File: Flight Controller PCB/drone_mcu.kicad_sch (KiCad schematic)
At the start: 24 parts, among them J2 JTAG, SW1 SW_Push, SW2 SW_SPDT, U2 STM32F411RETx, Y1 32.768kHz, Y2 25MHz

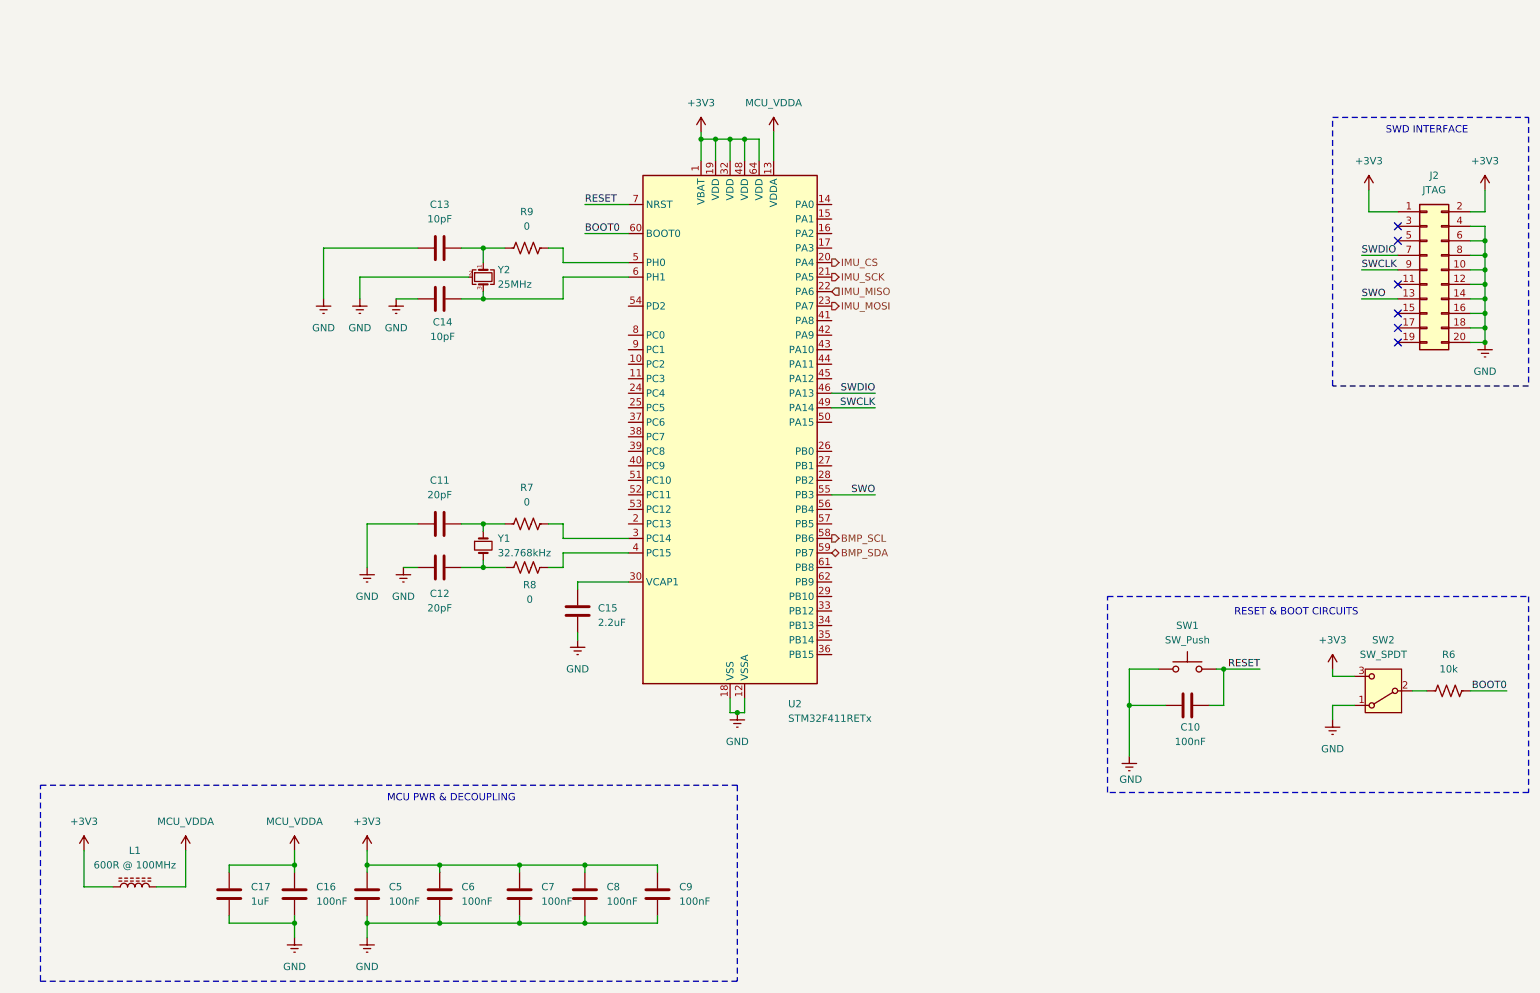
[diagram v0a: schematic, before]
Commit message: Selected motor controller, fixed MCU schematic and added I2C pullups
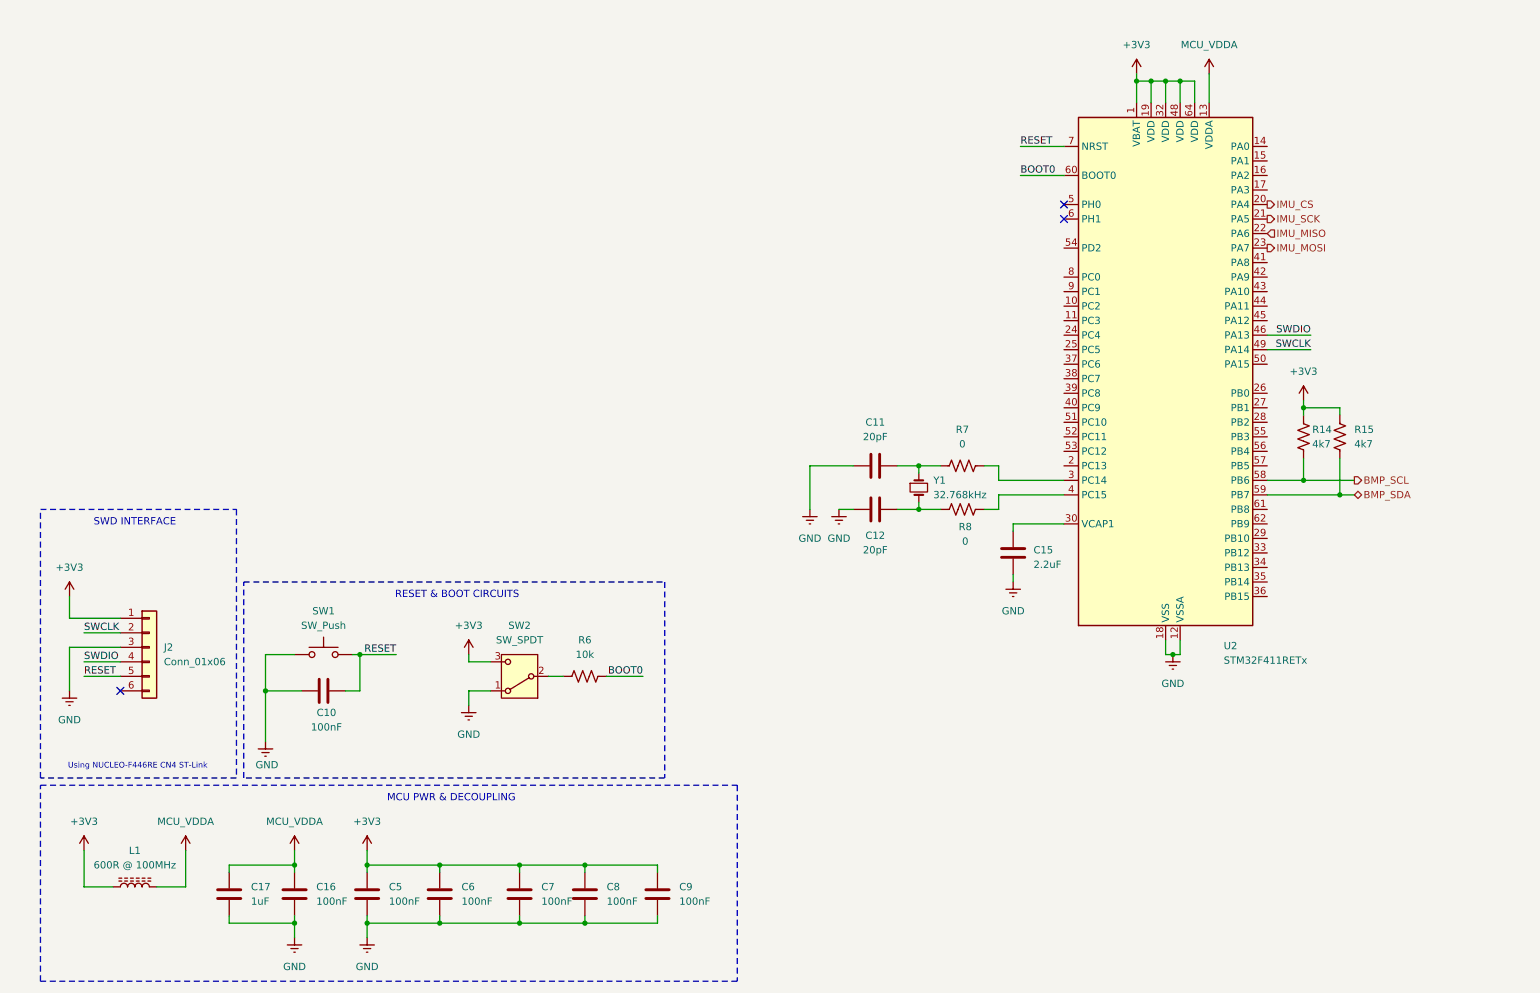
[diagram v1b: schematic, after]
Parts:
- removed C13, C14: 10pF, Capacitor_SMD:C_0603_1608Metric, symbol Device:C
- removed J2: JTAG, Connector_PinSocket_2.54mm:PinSocket_2x10_P2.54mm_Vertical_SMD, symbol Connector_Generic:Conn_02x10_Odd_Even
- removed R9: 0, Resistor_SMD:R_0603_1608Metric, symbol Device:R_US
- removed Y2: 25MHz, Crystal:Crystal_SMD_3225-4Pin_3.2x2.5mm, symbol Device:Crystal_GND24_Small
- added J2: Conn_01x06, symbol Connector_Generic:Conn_01x06
- added R14, R15: 4k7, Resistor_SMD:R_0603_1608Metric, symbol Device:R_US
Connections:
- net +3V3: now also J2.1 (Pin_1), R14.2, R15.2
- net BMP_SCL: now also R14.1
- net BMP_SDA: now also R15.1
- net GND: now also J2.3 (Pin_3)
- net RESET: now also J2.5 (Pin_5)
- net SWCLK: now also J2.2 (Pin_2)
- net SWDIO: now also J2.4 (Pin_4)
- net SWO: no longer names the net of U2.55 (PB3)
- no-connect marks 6 -> 3
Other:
- note added: "Using NUCLEO-F446RE CN4 ST-Link"
- moved on the sheet: C10, C11, C12, C15, R6, R7, R8, SW1, SW2, U2, Y1

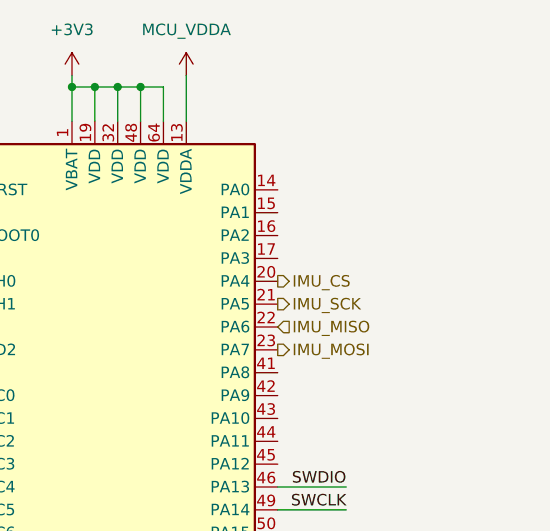
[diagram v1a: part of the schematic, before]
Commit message: Some changes. TODO: Add power and control for RunCam2. Add battery voltage monitoring
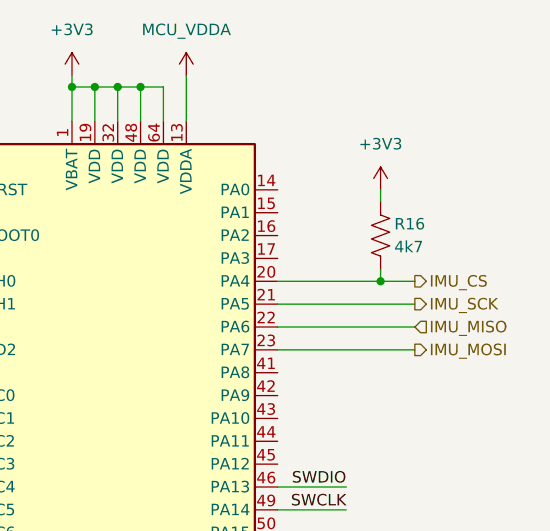
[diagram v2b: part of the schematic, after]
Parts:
- added R16: 4k7, Resistor_SMD:R_0603_1608Metric, symbol Device:R_US
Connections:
- net +3V3: now also R16.2
- net IMU_CS: now also R16.1
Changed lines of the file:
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@@
 	)
 	(junction
+		(at 245.11 55.88)
+		(diameter 0)
+		(color 0 0 0 0)
+	)
+	(junction
 		(at 63.5 181.61)
 		(diameter 0)
@@
 	(wire
 		(pts
+			(xy 248.92 58.42) (xy 233.68 58.42)
+		)
+		(stroke
+			(width 0)
+			(type default)
+		)
+	)
+	(wire
+		(pts
 			(xy 63.5 171.45) (xy 63.5 172.72)
 		)
@@
 	(wire
 		(pts
+			(xy 248.92 60.96) (xy 233.68 60.96)
+		)
+		(stroke
+			(width 0)
+			(type default)
+		)
+	)
+	(wire
+		(pts
 			(xy 24.13 128.27) (xy 33.02 128.27)
 		)
@@
 	(wire
 		(pts
+			(xy 233.68 55.88) (xy 245.11 55.88)
+		)
+		(stroke
+			(width 0)
+			(type default)
+		)
+	)
+	(wire
+		(pts
 			(xy 240.03 104.14) (xy 248.92 104.14)
 		)
@@
 	(wire
 		(pts
+			(xy 248.92 63.5) (xy 233.68 63.5)
+		)
+		(stroke
+			(width 0)
+			(type default)
+		)
+	)
+	(wire
+		(pts
 			(xy 127 181.61) (xy 127 180.34)
 		)
@@
 	(wire
 		(pts
+			(xy 248.92 55.88) (xy 245.11 55.88)
+		)
+		(stroke
+			(width 0)
+			(type default)
+		)
+	)
+	(wire
+		(pts
 			(xy 240.03 100.33) (xy 240.03 104.14)
 		)
@@
 	(wire
 		(pts
+			(xy 245.11 54.61) (xy 245.11 55.88)
+		)
+		(stroke
+			(width 0)
+			(type default)
+		)
+	)
+	(wire
+		(pts
 			(xy 189.23 111.76) (xy 198.12 111.76)
 		)
@@
 	(wire
 		(pts
+			(xy 245.11 45.72) (xy 245.11 46.99)
+		)
+		(stroke
+			(width 0)
+			(type default)
+		)
+	)
+	(wire
+		(pts
 			(xy 102.87 171.45) (xy 114.3 171.45)
 		)
@@
 	(hierarchical_label "IMU_SCK"
 		(shape output)
-		(at 233.68 58.42 0)
+		(at 248.92 58.42 0)
 		(effects
 			(font
@@
 	(hierarchical_label "IMU_CS"
 		(shape output)
-		(at 233.68 55.88 0)
+		(at 248.92 55.88 0)
 		(effects
 			(font
@@
 	(hierarchical_label "IMU_MOSI"
 		(shape output)
-		(at 233.68 63.5 0)
+		(at 248.92 63.5 0)
 		(effects
 			(font
@@
 	(hierarchical_label "IMU_MISO"
 		(shape input)
-		(at 233.68 60.96 0)
+		(at 248.92 60.96 0)
 		(effects
 			(font
@@
 	(symbol
 		(lib_id "Device:R_US")
+		(at 245.11 50.8 180)
+		(unit 1)
+		(body_style 1)
+		(exclude_from_sim no)
+		(in_bom yes)
+		(on_board yes)
+		(in_pos_files yes)
+		(dnp no)
+		(property "Reference" "R16"
+			(at 246.634 49.53 0)
+			(show_name no)
+			(do_not_autoplace no)
+			(effects
+				(font
+					(size 1.27 1.27)
+				)
+				(justify right)
+			)
+		)
+		(property "Value" "4k7"
+			(at 246.634 52.07 0)
+			(show_name no)
+			(do_not_autoplace no)
+			(effects
+				(font
+					(size 1.27 1.27)
+				)
+				(justify right)
+			)
+		)
+		(property "Footprint" "Resistor_SMD:R_0603_1608Metric"
+			(at 244.094 50.546 90)
+			(hide yes)
+			(show_name no)
+			(do_not_autoplace no)
+			(effects
+				(font
+					(size 1.27 1.27)
+				)
+			)
+		)
+		(property "Datasheet" ""
+			(at 245.11 50.8 0)
+			(hide yes)
+			(show_name no)
+			(do_not_autoplace no)
+			(effects
+				(font
+					(size 1.27 1.27)
+				)
+			)
+		)
+		(property "Description" "Resistor, US symbol"
+			(at 245.11 50.8 0)
+			(hide yes)
+			(show_name no)
+			(do_not_autoplace no)
+			(effects
+				(font
+					(size 1.27 1.27)
+				)
+			)
+		)
+		(pin "1"
+		)
+		(pin "2"
+		)
+		(instances
+			(project "Drone Board"
+				(path "/11d338fc-6b4d-4a31-a103-caeefef24b64/8be55338-8553-4645-bbc6-3c82c168951e"
+					(reference "R16")
+					(unit 1)
+				)
+			)
+		)
+	)
+	(symbol
+		(lib_id "Device:R_US")
 		(at 180.34 101.6 90)
 		(unit 1)
@@
 					(unit 1)
 				)
+			)
+		)
+	)
+	(symbol
+		(lib_id "power:+3V3")
+		(at 245.11 45.72 0)
+		(unit 1)
+		(body_style 1)
+		(exclude_from_sim no)
+		(in_bom yes)
+		(on_board yes)
+		(in_pos_files yes)
+		(dnp no)
+		(fields_autoplaced yes)
+		(property "Reference" "#PWR051"
+			(at 245.11 49.53 0)
+			(hide yes)
+			(show_name no)
+			(do_not_autoplace no)
+			(effects
+				(font
+					(size 1.27 1.27)
+				)
+			)
+		)
+		(property "Value" "+3V3"
+			(at 245.11 40.64 0)
+			(show_name no)
+			(do_not_autoplace no)
+			(effects
+				(font
+					(size 1.27 1.27)
+				)
+			)
+		)
+		(property "Footprint" ""
+			(at 245.11 45.72 0)
+			(hide yes)
+			(show_name no)
+			(do_not_autoplace no)
+			(effects
+				(font
+					(size 1.27 1.27)
+				)
+			)
+		)
+		(property "Datasheet" ""
+			(at 245.11 45.72 0)
+			(hide yes)
+			(show_name no)
+			(do_not_autoplace no)
+			(effects
+				(font
+					(size 1.27 1.27)
+				)
+			)
+		)
+		(property "Description" "Power symbol creates a global label with name \"+3V3\""
+			(at 245.11 45.72 0)
+			(hide yes)
+			(show_name no)
+			(do_not_autoplace no)
+			(effects
+				(font
+					(size 1.27 1.27)
+				)
+			)
+		)
+		(pin "1"
+		)
+		(instances
+			(project "Drone Board"
+				(path "/11d338fc-6b4d-4a31-a103-caeefef24b64/8be55338-8553-4645-bbc6-3c82c168951e"
+					(reference "#PWR051")
+					(unit 1)
+				)

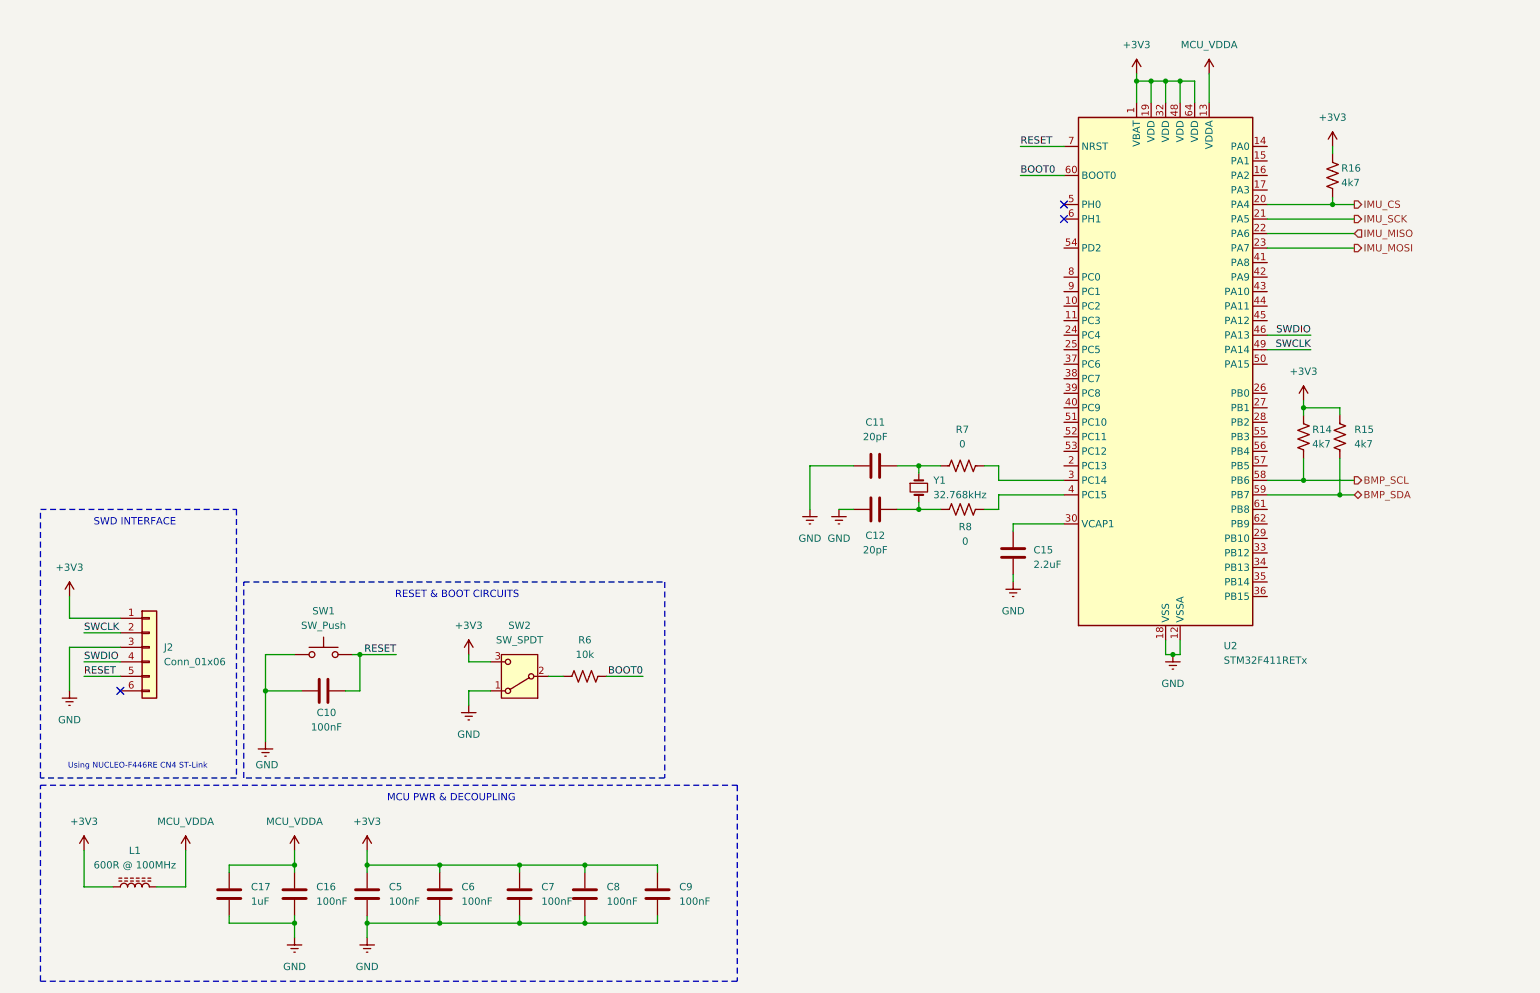
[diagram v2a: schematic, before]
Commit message: Finished converters, combined converter & sensor sheets. Updated I2C & CS pullups. TODO: Add motor control pins to MCU & control pins for camera
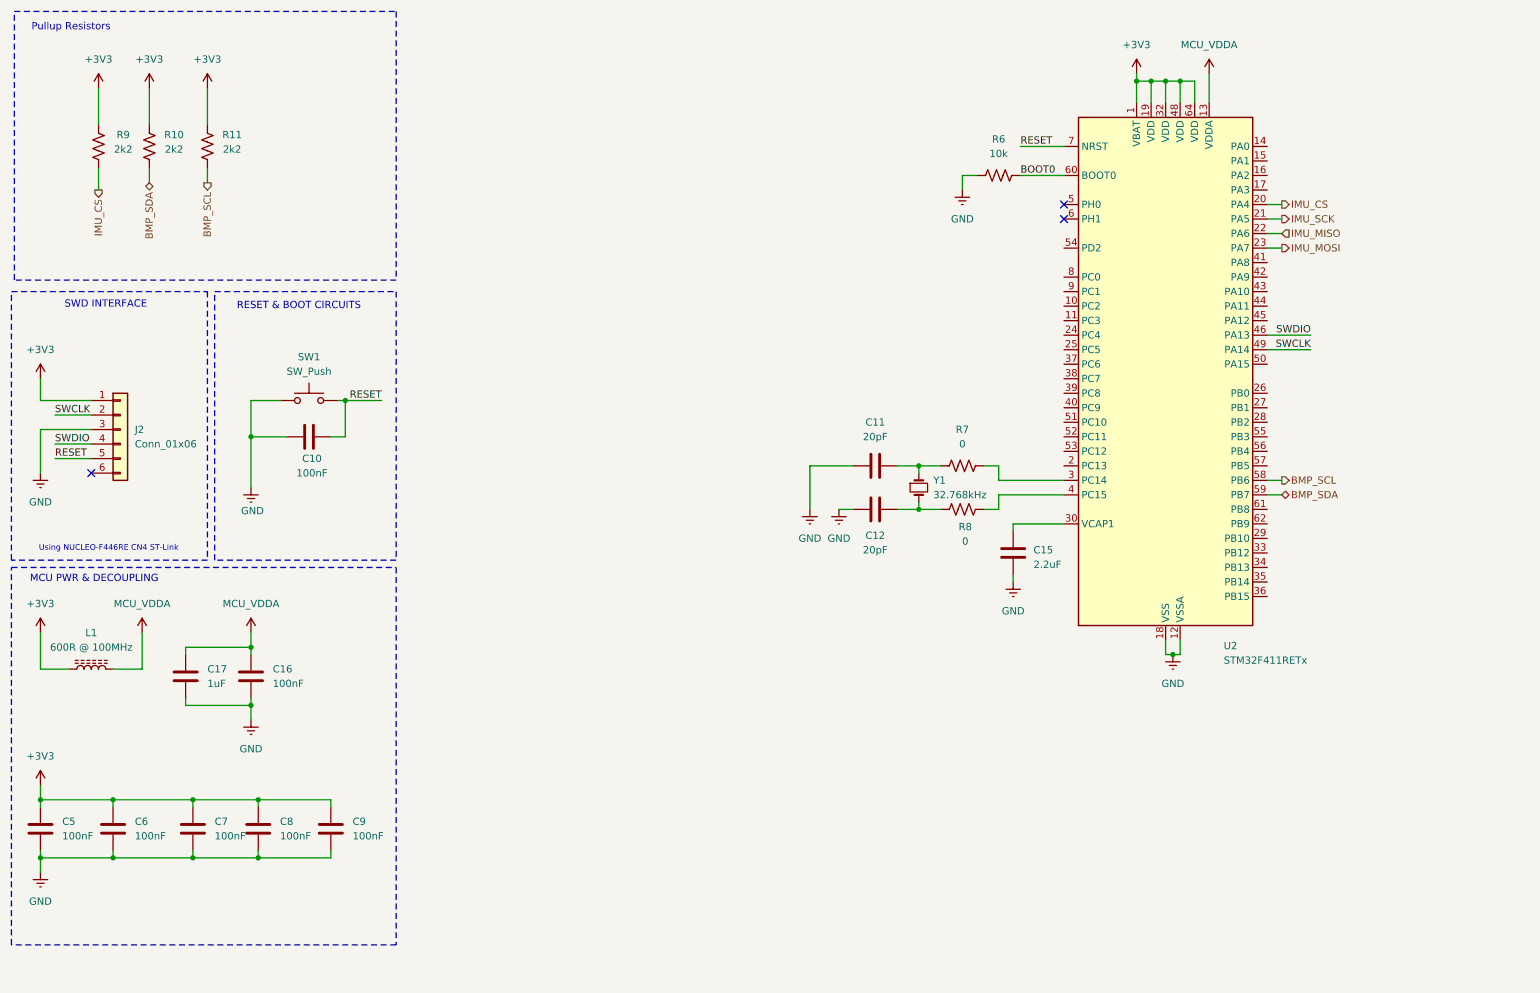
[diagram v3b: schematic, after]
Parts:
- removed R14, R15, R16: 4k7, Resistor_SMD:R_0603_1608Metric, symbol Device:R_US
- removed SW2: SW_SPDT, Drone_Fp:SW_EG1213, symbol Switch:SW_SPDT
- added R10, R11, R9: 2k2, Resistor_SMD:R_0603_1608Metric, symbol Device:R_US
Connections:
- net +3V3: now also R10.2, R11.2, R9.2
- net BMP_SCL: now also R11.1
- net BMP_SDA: now also R10.1
- net GND: now also R6.1
- net IMU_CS: now also R9.1
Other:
- note added: "Pullup Resistors"
- moved on the sheet: C10, C16, C17, C5, C6, C7, C8, C9, J2, L1, R6, SW1

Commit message: Init
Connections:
- net VCAP1: now reaches C15.1, U2.30 (VCAP1)
- net CRYS_1: now reaches R7.2, U2.3 (PC14)
- net CRYS_2: now reaches R8.2, U2.4 (PC15)
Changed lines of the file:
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@@
 	(paper "A4")
 	(rectangle
-		(start 14.478 22.098)
+		(start 13.97 22.098)
 		(end 81.28 69.088)
 		(stroke
@@
 		)
 	)
+	(label "CRYS_1"
+		(at 186.69 104.14 0)
+		(effects
+			(font
+				(size 1.27 1.27)
+			)
+			(justify left bottom)
+		)
+	)
 	(label "SWCLK"
 		(at 241.3 81.28 180)
@@
 		)
 	)
+	(label "VCAP1"
+		(at 189.23 111.76 0)
+		(effects
+			(font
+				(size 1.27 1.27)
+			)
+			(justify left bottom)
+		)
+	)
 	(label "SWDIO"
 		(at 241.3 78.74 180)
@@
 		(effects
 			(font
+				(size 1.27 1.27)
+			)
+			(justify left bottom)
+		)
+	)
+	(label "CRYS_2"
+		(at 186.69 106.68 0)
+		(effects
+			(font
